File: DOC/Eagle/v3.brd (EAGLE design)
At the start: 55 x 59 mm, 26 parts, among them IC1 ADPS-9200, IC2 PIC12LF1552, IC3 M24C01/02-XTSSOP08, M1 RF-LORA-868-SO, X1 SMA-142-0701-871/876

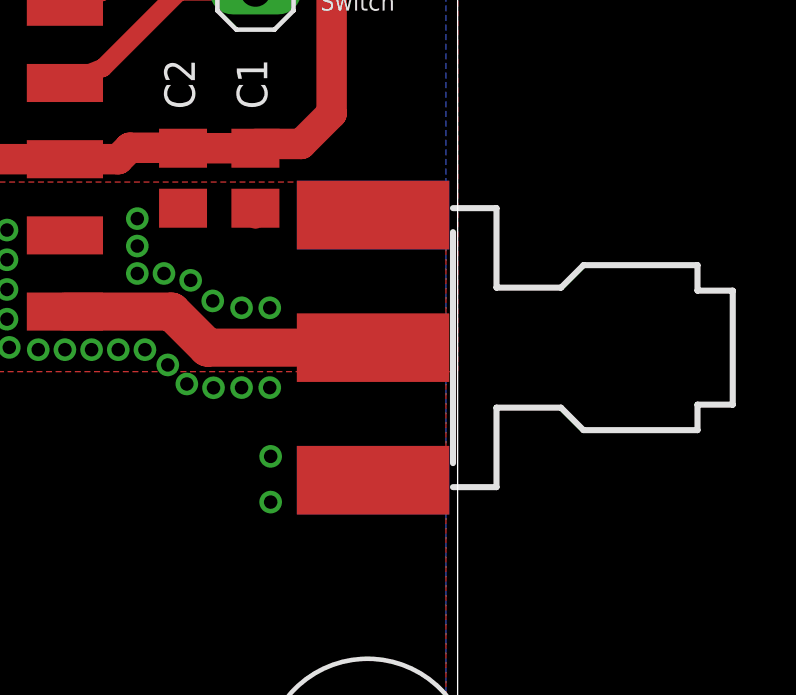
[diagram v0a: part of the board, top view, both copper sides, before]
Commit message: Updated component list
1) Fixed wrong component name for APDS-9200
2) Added possible suppliers to the partlist
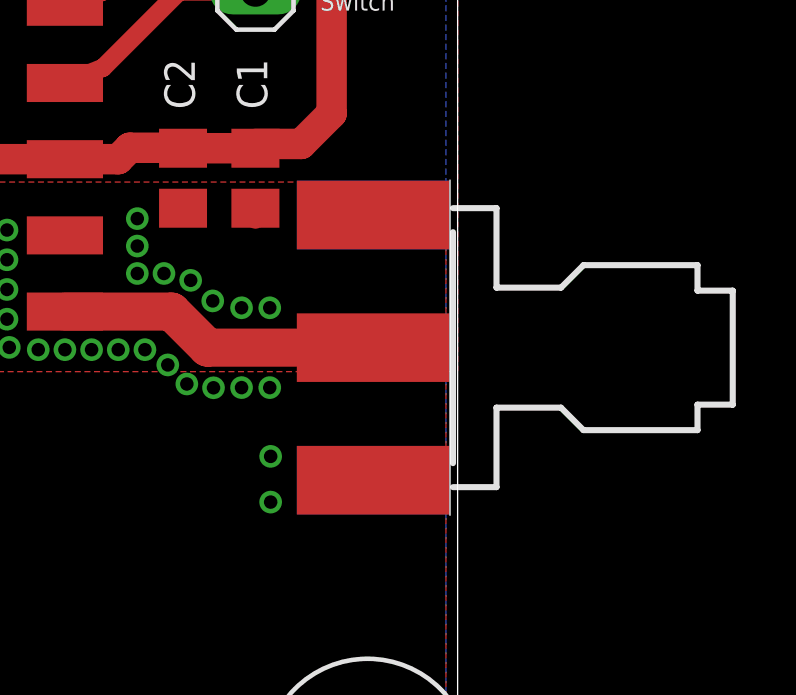
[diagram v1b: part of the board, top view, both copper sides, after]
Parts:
- IC1: value ADPS-9200 -> APDS-9200; device project:ADPS-9200 -> project:APDS-9200
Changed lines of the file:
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@@
 </autorouter>
 <elements>
-<element name="C1" library="rcl" package="C0805K" value="10n" x="48.26" y="22.447" smashed="yes" rot="R270">
+<element name="C1" library="rcl" library_urn="urn:adsk.eagle:library:334" package="C0805K" value="10n" x="48.26" y="22.447" smashed="yes" rot="R270">
 <attribute name="NAME" x="48.655" y="24.749" size="1.016" layer="25" font="vector" rot="R90"/>
 <attribute name="VALUE" x="46.36" y="23.447" size="1.016" layer="27" rot="R270"/>
 </element>
-<element name="C2" library="rcl" package="C0805K" value="100n" x="45.847" y="22.447" smashed="yes" rot="R270">
+<element name="C2" library="rcl" library_urn="urn:adsk.eagle:library:334" package="C0805K" value="100n" x="45.847" y="22.447" smashed="yes" rot="R270">
 <attribute name="NAME" x="46.242" y="24.749" size="1.016" layer="25" font="vector" rot="R90"/>
 <attribute name="VALUE" x="43.947" y="23.447" size="1.016" layer="27" rot="R270"/>
@@
 <element name="JP1" library="project" package="SMH-110-X2-XX-D" value="SMH-110-X2-XX-D" x="11" y="29.5" smashed="yes" rot="R270"/>
 <element name="M1" library="project" package="RF-LORA-868-SO" value="RF-LORA-868-SO" x="33.02" y="26.892" smashed="yes" rot="R180"/>
-<element name="X1" library="con-coax" package="J502-ND-142-0701-871/876" value="SMA-142-0701-871/876" x="54.746" y="16.8" smashed="yes" rot="R180">
+<element name="X1" library="con-coax" library_urn="urn:adsk.eagle:library:133" package="J502-ND-142-0701-871/876" value="SMA-142-0701-871/876" x="54.746" y="16.8" smashed="yes" rot="R180">
 <attribute name="MF" value="JOHNSON COMPONENTS" x="54.746" y="16.8" size="1.778" layer="27" rot="R180" display="off"/>
 <attribute name="MPN" value="142-0701-871" x="54.746" y="16.8" size="1.778" layer="27" rot="R180" display="off"/>
@@
 <attribute name="OC_NEWARK" value="91B6105" x="54.746" y="16.8" size="1.778" layer="27" rot="R180" display="off"/>
 </element>
-<element name="R1" library="rcl" package="M0805" value="10k" x="25.4" y="47.72" smashed="yes" rot="R270">
+<element name="R1" library="rcl" library_urn="urn:adsk.eagle:library:334" package="M0805" value="10k" x="25.4" y="47.72" smashed="yes" rot="R270">
 <attribute name="NAME" x="23.368" y="48.482" size="0.8128" layer="25" font="vector" rot="R270"/>
 </element>
-<element name="R2" library="rcl" package="M0805" value="10k" x="27.432" y="47.72" smashed="yes" rot="R270">
+<element name="R2" library="rcl" library_urn="urn:adsk.eagle:library:334" package="M0805" value="10k" x="27.432" y="47.72" smashed="yes" rot="R270">
 <attribute name="NAME" x="28.702" y="48.482" size="0.8128" layer="25" font="vector" rot="R270"/>
 </element>
-<element name="R3" library="rcl" package="M0805" value="10k" x="18.034" y="47.72" smashed="yes" rot="R270">
+<element name="R3" library="rcl" library_urn="urn:adsk.eagle:library:334" package="M0805" value="10k" x="18.034" y="47.72" smashed="yes" rot="R270">
 <attribute name="NAME" x="19.304" y="48.482" size="0.8128" layer="25" font="vector" rot="R270"/>
 </element>
-<element name="C5" library="rcl" package="C0805K" value="1u" x="26.416" y="53.816" smashed="yes" rot="R90">
+<element name="C5" library="rcl" library_urn="urn:adsk.eagle:library:334" package="C0805K" value="1u" x="26.416" y="53.816" smashed="yes" rot="R90">
 <attribute name="NAME" x="28.589" y="53.07" size="0.8128" layer="25" font="vector" rot="R90"/>
 </element>
-<element name="JP2" library="pinhead" package="1X03" value="" x="12.7" y="48.99" smashed="yes" rot="R270">
+<element name="JP2" library="pinhead" library_urn="urn:adsk.eagle:library:325" package="1X03" value="" x="12.7" y="48.99" smashed="yes" rot="R270">
 <attribute name="VALUE" x="9.525" y="52.8" size="1.27" layer="27" rot="R270"/>
 </element>
-<element name="JP3" library="pinhead" package="1X06" value="" x="33.02" y="42.64" smashed="yes">
+<element name="JP3" library="pinhead" library_urn="urn:adsk.eagle:library:325" package="1X06" value="" x="33.02" y="42.64" smashed="yes">
 <attribute name="VALUE" x="25.4" y="39.465" size="1.27" layer="27"/>
 </element>
-<element name="JP4" library="pinhead" package="1X04" value="" x="17.907" y="21.812" smashed="yes" rot="R90">
+<element name="JP4" library="pinhead" library_urn="urn:adsk.eagle:library:325" package="1X04" value="" x="17.907" y="21.812" smashed="yes" rot="R90">
 <attribute name="VALUE" x="21.082" y="16.732" size="1.27" layer="27" rot="R90"/>
 </element>
-<element name="JP5" library="pinhead" package="1X05" value="" x="48.26" y="33.75" smashed="yes" rot="R270">
+<element name="JP5" library="pinhead" library_urn="urn:adsk.eagle:library:325" package="1X05" value="" x="48.26" y="33.75" smashed="yes" rot="R270">
 <attribute name="VALUE" x="45.085" y="40.1" size="1.27" layer="27" rot="R270"/>
 </element>
-<element name="IC1" library="project" package="ADPS-9200" value="ADPS-9200" x="23.114" y="51.53" smashed="yes" rot="R90">
+<element name="IC1" library="project" package="APDS-9200" value="APDS-9200" x="23.114" y="51.53" smashed="yes" rot="R90">
 <attribute name="NAME" x="22.368" y="53.138" size="0.8128" layer="25" font="vector"/>
 </element>
-<element name="H1" library="holes" package="3,0" value="MOUNT-HOLE3.0" x="3" y="3"/>
-<element name="H2" library="holes" package="3,0" value="MOUNT-HOLE3.0" x="52" y="3"/>
-<element name="H4" library="holes" package="3,0" value="MOUNT-HOLE3.0" x="3" y="56"/>
-<element name="H3" library="holes" package="3,0" value="MOUNT-HOLE3.0" x="52" y="56"/>
+<element name="H1" library="holes" library_urn="urn:adsk.eagle:library:237" package="3,0" value="MOUNT-HOLE3.0" x="3" y="3"/>
+<element name="H2" library="holes" library_urn="urn:adsk.eagle:library:237" package="3,0" value="MOUNT-HOLE3.0" x="52" y="3"/>
+<element name="H4" library="holes" library_urn="urn:adsk.eagle:library:237" package="3,0" value="MOUNT-HOLE3.0" x="3" y="56"/>
+<element name="H3" library="holes" library_urn="urn:adsk.eagle:library:237" package="3,0" value="MOUNT-HOLE3.0" x="52" y="56"/>
 <element name="JP6" library="project" package="1X06/SMD" value="PICKIT-HEADERSMD-PADS" x="37.338" y="56.467" smashed="yes" rot="MR0"/>
 <element name="IC2" library="project" package="MSOP8" value="PIC12LF1552" x="36.068" y="50.768" smashed="yes" rot="R90">
 <attribute name="NAME" x="37.25" y="53.19" size="0.8128" layer="25" font="vector" rot="R180"/>
 </element>
-<element name="C3" library="rcl" package="C0805K" value="100n" x="36.068" y="48.482" smashed="yes" rot="R180">
+<element name="C3" library="rcl" library_urn="urn:adsk.eagle:library:334" package="C0805K" value="100n" x="36.068" y="48.482" smashed="yes" rot="R180">
 <attribute name="NAME" x="36.814" y="47.099" size="0.8128" layer="25" font="vector" rot="R180"/>
 </element>
-<element name="C4" library="rcl" package="C0805K" value="100n" x="43.942" y="48.482" smashed="yes">
+<element name="C4" library="rcl" library_urn="urn:adsk.eagle:library:334" package="C0805K" value="100n" x="43.942" y="48.482" smashed="yes">
 <attribute name="NAME" x="43.196" y="46.563" size="0.8128" layer="25" font="vector"/>
 </element>
@@
 <attribute name="VALUE" x="50.8" y="45.688" size="1.27" layer="27" rot="R90"/>
 </element>
-<element name="R4" library="rcl" package="M0805" value="3k3" x="48.26" y="43.402" smashed="yes" rot="R270">
+<element name="R4" library="rcl" library_urn="urn:adsk.eagle:library:334" package="M0805" value="3k3" x="48.26" y="43.402" smashed="yes" rot="R270">
 <attribute name="NAME" x="49.53" y="44.164" size="0.8128" layer="25" font="vector" rot="R270"/>
 </element>
-<element name="R5" library="rcl" package="M0805" value="6k8" x="43.942" y="53.562" smashed="yes">
+<element name="R5" library="rcl" library_urn="urn:adsk.eagle:library:334" package="M0805" value="6k8" x="43.942" y="53.562" smashed="yes">
 <attribute name="NAME" x="43.18" y="54.832" size="0.8128" layer="25" font="vector"/>
 </element>
